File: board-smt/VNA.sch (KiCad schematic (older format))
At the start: 80 parts, among them J1 Conn_02x07_Odd_Even, J10 Conn_01x01, J11 Conn_01x01, J12 Conn_01x01, J13 Barrel_Jack, J14 Conn_01x01, J15 Conn_02x05_Odd_Even, J16 Conn_01x01, J17 Conn_01x04, J18 Conn_01x01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

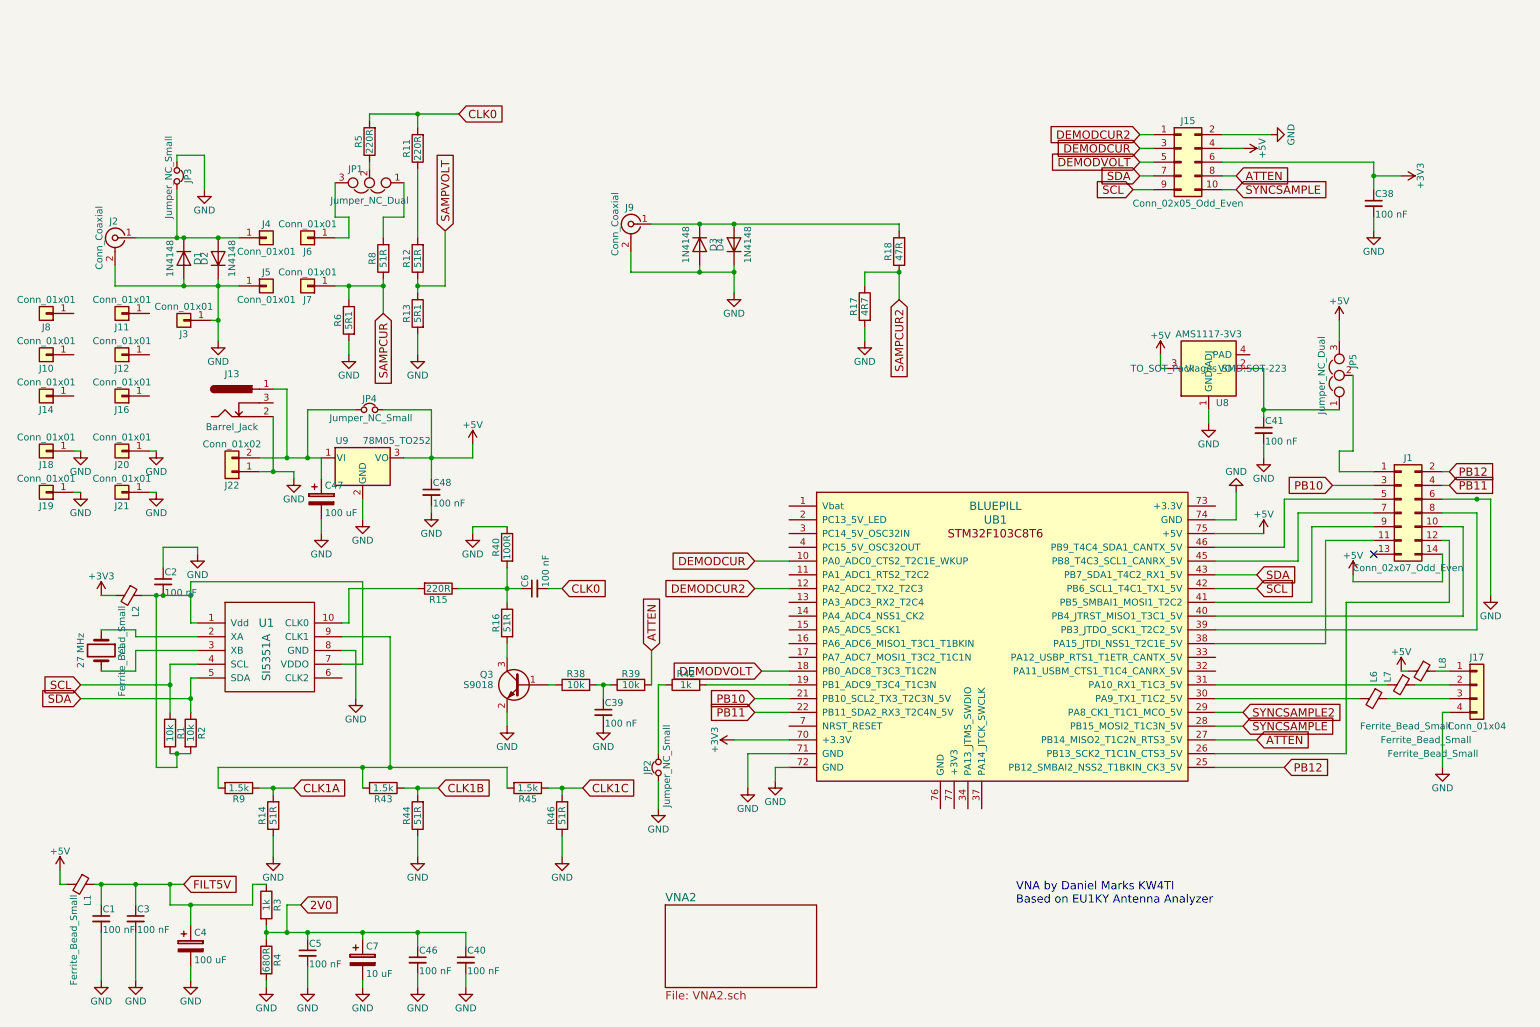
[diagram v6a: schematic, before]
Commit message: Added JST 2.54 power and USB-B connecotrs
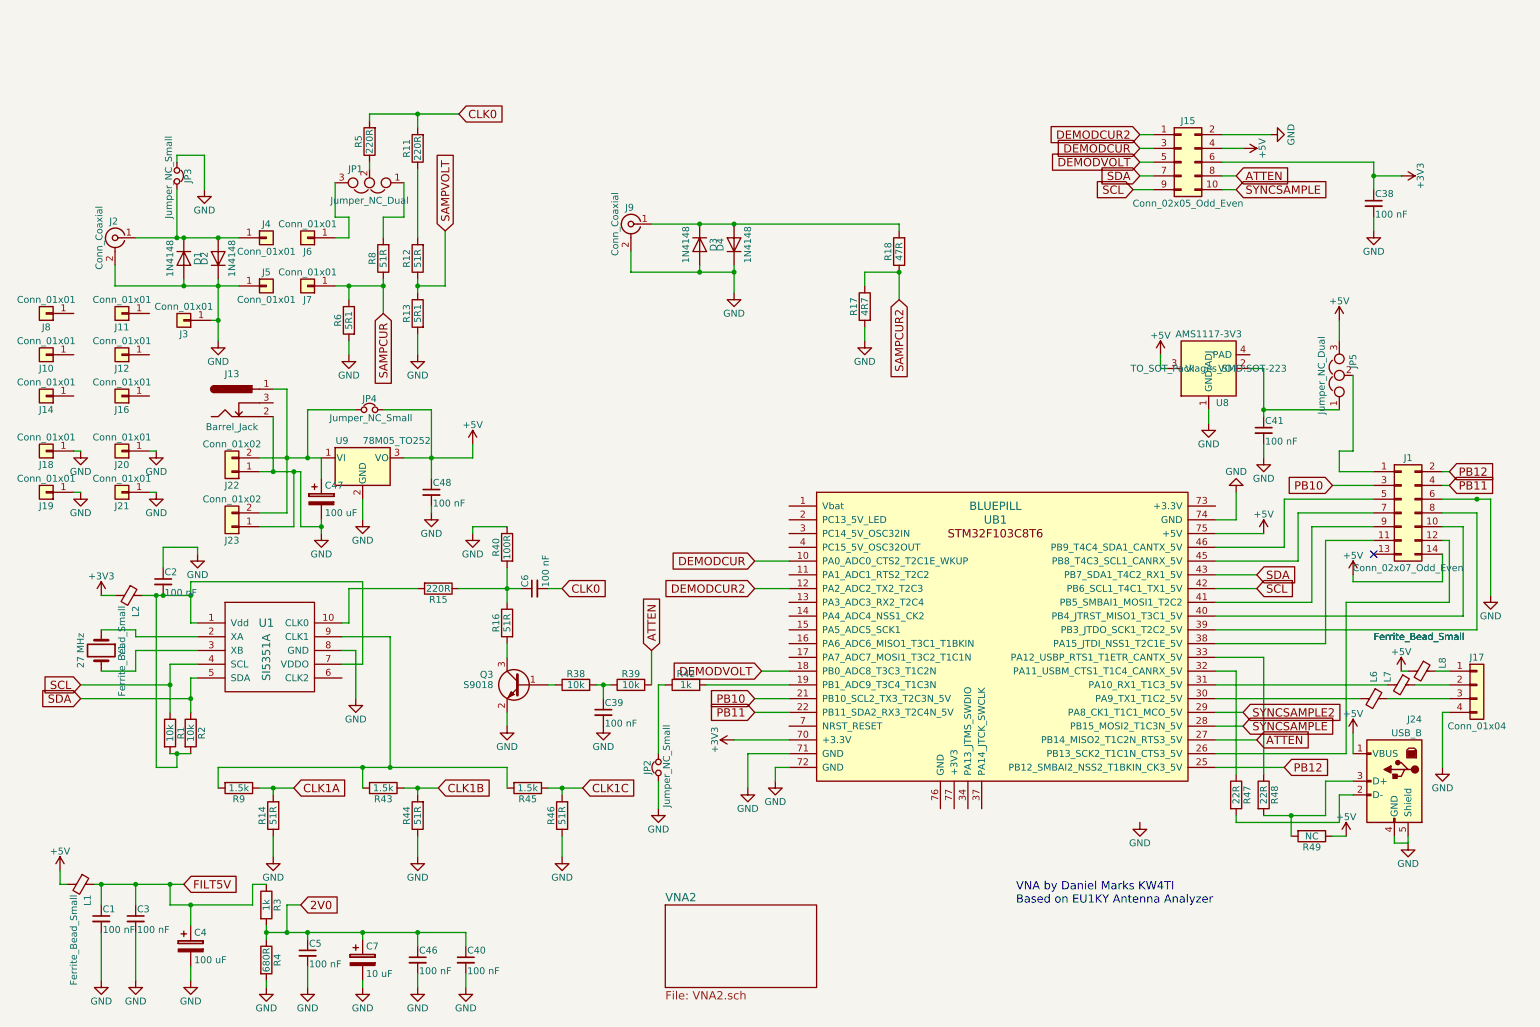
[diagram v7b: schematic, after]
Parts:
- added J23: Conn_01x02, Connectors_Molex:Molex_KK-6410-02_02x2.54mm_Straight, symbol Conn_01x02
- added J24: USB_B, Connectors:USB_B, symbol USB_B
- added R47, R48: 22R, Resistors_SMD:R_0805_HandSoldering, symbol R
- added R49: NC, Resistors_SMD:R_0805_HandSoldering, symbol R
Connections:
- net +5V: now also J24.1 (VBUS), R49.1
- net GND: now also J23.1 (Pin_1), J24.4 (GND), J24.5 (Shield)
- net at UB1.32 (PA11_USBM_CTS1_T1C4_CANRX_5V): now also R47.1
- net at UB1.33 (PA12_USBP_RTS1_T1ETR_CANTX_5V): now also R48.1
- net at C47.1, J13.1, J22.2 (Pin_2)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: now also J23.2 (Pin_2)
- new net: J24.2 (D-), R47.2
- new net: J24.3 (D+), R48.2, R49.2

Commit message: Added mt3608 boost converter for battery usage
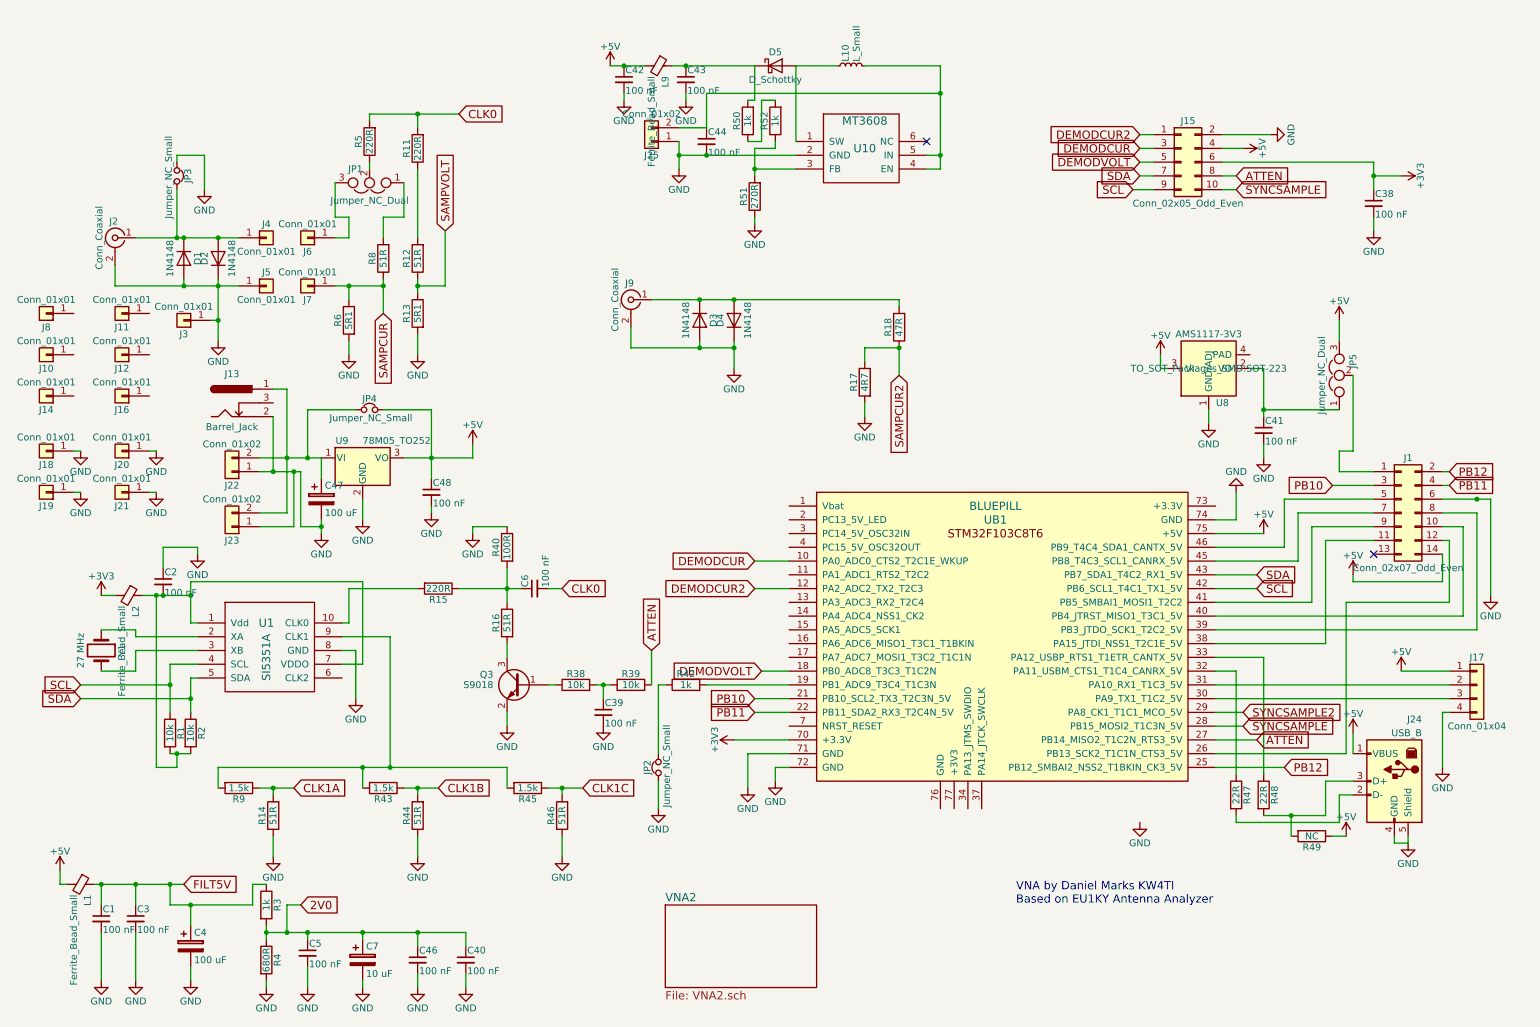
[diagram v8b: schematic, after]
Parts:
- removed L6, L7, L8: Ferrite_Bead_Small, Inductors_SMD:L_0805_HandSoldering, symbol Ferrite_Bead_Small
- added C42, C43, C44: 100 nF, Capacitors_SMD:C_0805_HandSoldering, symbol C_Small
- added D5: D_Schottky, Diodes_SMD:D_SOD-123, symbol D_Schottky
- added J25: Conn_01x02, Connectors_Molex:Molex_KK-6410-02_02x2.54mm_Straight, symbol Conn_01x02
- added L10: L_Small, Inductors_SMD:L_7.3x7.3_H4.5, symbol L_Small
- added L9: Ferrite_Bead_Small, Inductors_SMD:L_1206_HandSoldering, symbol Ferrite_Bead_Small
- added R50, R52: 1k, Resistors_SMD:R_0805_HandSoldering, symbol R
- added R51: 270R, Resistors_SMD:R_0805_HandSoldering, symbol R
- added U10: MT3608, TO_SOT_Packages_SMD:SOT-23-6, symbol MT3608
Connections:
- net +5V: now also J17.1 (Pin_1), C42.1, L9.2
- net GND: now also C42.2, C43.2, C44.2, J25.1 (Pin_1), R51.1, U10.2 (GND)
- net at UB1.30 (PA9_TX1_T1C2_5V): now also J17.3 (Pin_3)
- net at UB1.31 (PA10_RX1_T1C3_5V): now also J17.2 (Pin_2)
- new net: C44.1, J25.2 (Pin_2), L10.2, U10.4 (EN), U10.5 (IN)
- new net: D5.2 (A), L10.1, U10.1 (SW)
- new net: R51.2, R52.1, U10.3 (FB)
- new net: C43.1, D5.1 (K), L9.1, R50.2
- new net: R50.1, R52.2
- no-connect marks 1 -> 2
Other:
- moved on the sheet: D3, D4, J9, R17, R18
